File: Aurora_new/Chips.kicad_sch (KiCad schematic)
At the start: 87 parts, among them J1 UJ20-C-H-C-3-SMT-TR, J16 PPPC042LFBN-RC, J3 PPPC042LFBN-RC, J36 PPPC042LFBN-RC, J41 STEMMA QT, J50 PCB.RPSMAFRA.HT, J6 DM3AT-SF-PEJM5, U1 STM32H757BITx, U13 XBP9X-DMUS-001, U14 MS5611-01BA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

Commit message: added breakouts for xb and stlink
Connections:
- net 3V3: no longer D5.4 (VDD)
- net 3V3_MCU: now also D5.4 (VDD)
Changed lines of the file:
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@@
 	)
 	(global_label "V_OUT"
-		(shape output)
+		(shape bidirectional)
 		(at 562.61 137.16 0)
 		(fields_autoplaced yes)
@@
 		)
 		(property "Intersheetrefs" "${INTERSHEET_REFS}"
-			(at 571.28 137.16 0)
+			(at 572.3913 137.16 0)
 			(effects
 				(font
@@
 		)
 	)
-	(global_label "3V3"
+	(global_label "3V3_MCU"
 		(shape input)
 		(at 26.67 248.92 180)
@@
 		)
 		(property "Intersheetrefs" "${INTERSHEET_REFS}"
-			(at 20.1772 248.92 0)
-			(effects
-				(font
+			(at 15.1577 248.92 0)
+			(effects
+				(font

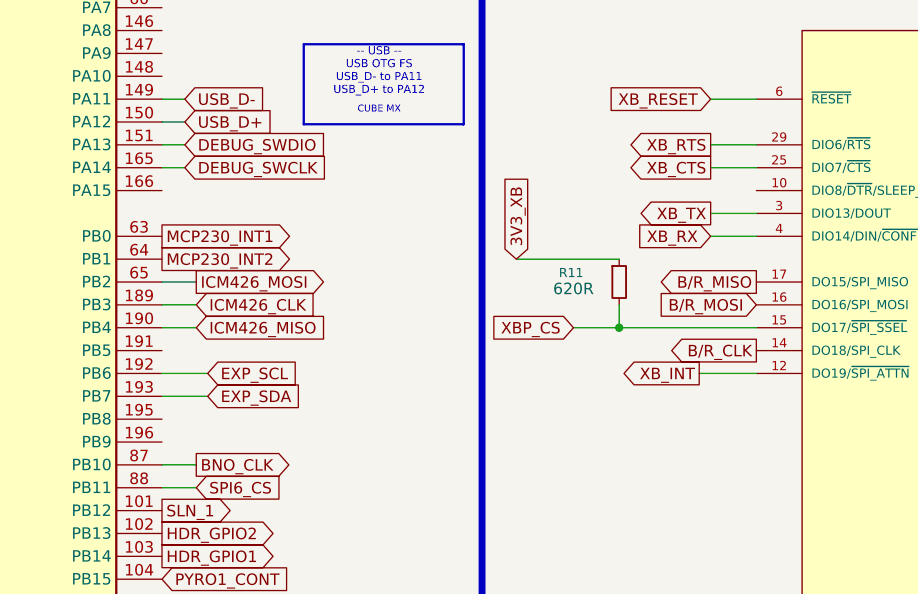
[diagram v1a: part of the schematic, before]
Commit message: fixed header pins, XB on UART
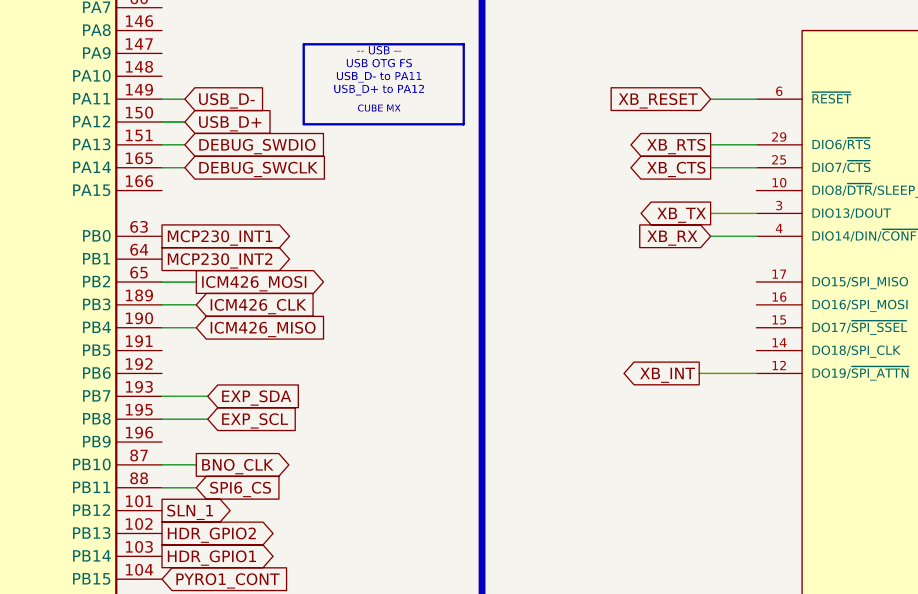
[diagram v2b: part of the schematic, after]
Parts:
- removed R11: 620R, Resistor_SMD:R_0805_2012Metric, symbol Device:R_Small
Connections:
- net B/R_CLK: no longer U13.14 (DO18/SPI_CLK)
- net B/R_MISO: no longer U13.17 (DO15/SPI_MISO)
- net B/R_MOSI: no longer U13.16 (DO16/SPI_MOSI)
- net EXP_SCL: now also U1.195 (PB8); no longer U1.192 (PB6)
- net XBP_CS: no longer U13.15 (DO17/~{SPI_SSEL})
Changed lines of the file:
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@@
 	)
 	(junction
-		(at 231.14 168.91)
-		(diameter 0)
-		(color 0 0 0 0)
-	)
-	(junction
 		(at 48.26 57.15)
 		(diameter 0)
@@
 	(wire
 		(pts
-			(xy 231.14 168.91) (xy 231.14 166.37)
-		)
-		(stroke
-			(width 0)
-			(type default)
-		)
-	)
-	(wire
-		(pts
 			(xy 478.79 341.63) (xy 478.79 347.98)
 		)
@@
 	(wire
 		(pts
-			(xy 231.14 168.91) (xy 246.38 168.91)
-		)
-		(stroke
-			(width 0)
-			(type default)
-		)
-	)
-	(wire
-		(pts
 			(xy 241.3 148.59) (xy 246.38 148.59)
 		)
@@
 	(wire
 		(pts
-			(xy 231.14 168.91) (xy 226.06 168.91)
-		)
-		(stroke
-			(width 0)
-			(type default)
-		)
-	)
-	(wire
-		(pts
 			(xy 38.1 49.53) (xy 40.64 49.53)
 		)
@@
 	(wire
 		(pts
-			(xy 180.34 173.99) (xy 185.42 173.99)
-		)
-		(stroke
-			(width 0)
-			(type default)
-		)
-	)
-	(wire
-		(pts
 			(xy 73.66 49.53) (xy 76.2 49.53)
 		)
@@
 	(wire
 		(pts
-			(xy 502.92 64.77) (xy 502.92 66.04)
+			(xy 180.34 179.07) (xy 185.42 179.07)
 		)
 		(stroke
@@
 	(wire
 		(pts
-			(xy 397.51 97.79) (xy 397.51 95.25)
+			(xy 502.92 64.77) (xy 502.92 66.04)
 		)
 		(stroke
@@
 	(wire
 		(pts
-			(xy 308.61 121.92) (xy 311.15 121.92)
+			(xy 397.51 97.79) (xy 397.51 95.25)
 		)
 		(stroke
@@
 	(wire
 		(pts
-			(xy 231.14 161.29) (xy 219.71 161.29)
+			(xy 308.61 121.92) (xy 311.15 121.92)
 		)
 		(stroke
@@
 		)
 	)
-	(global_label "B{slash}R_CLK"
-		(shape output)
-		(at 246.38 171.45 180)
-		(fields_autoplaced yes)
-		(effects
-			(font
-				(size 1.27 1.27)
-			)
-			(justify right)
-		)
-		(property "Intersheetrefs" "${INTERSHEET_REFS}"
-			(at 234.9886 171.45 0)
-			(effects
-				(font
-					(size 1.27 1.27)
-				)
-				(justify right)
-				(hide yes)
-			)
-		)
-	)
 	(global_label "BNO_NRST"
 		(shape output)
@@
 		)
 	)
-	(global_label "3V3_XB"
-		(shape input)
-		(at 219.71 161.29 90)
-		(fields_autoplaced yes)
-		(effects
-			(font
-				(size 1.27 1.27)
-			)
-			(justify left)
-		)
-		(property "Intersheetrefs" "${INTERSHEET_REFS}"
-			(at 219.71 151.3501 90)
-			(effects
-				(font
-					(size 1.27 1.27)
-				)
-				(justify left)
-				(hide yes)
-			)
-		)
-	)
 	(global_label "GPIO_B7"
 		(shape input)
@@
 		)
 	)
-	(global_label "XBP_CS"
-		(shape input)
-		(at 226.06 168.91 180)
-		(fields_autoplaced yes)
-		(effects
-			(font
-				(size 1.27 1.27)
-			)
-			(justify right)
-		)
-		(property "Intersheetrefs" "${INTERSHEET_REFS}"
-			(at 215.8782 168.91 0)
-			(effects
-				(font
-					(size 1.27 1.27)
-				)
-				(justify right)
-				(hide yes)
-			)
-		)
-	)
 	(global_label "3V3_SENS"
 		(shape input)
@@
 		)
 	)
-	(global_label "EXP_SCL"
-		(shape input)
-		(at 185.42 173.99 0)
-		(fields_autoplaced yes)
-		(effects
-			(font
-				(size 1.27 1.27)
-			)
-			(justify left)
-		)
-		(property "Intersheetrefs" "${INTERSHEET_REFS}"
-			(at 196.5089 173.99 0)
-			(effects
-				(font
-					(size 1.27 1.27)
-				)
-				(justify left)
-				(hide yes)
-			)
-		)
-	)
 	(global_label "ICM426_INT2"
 		(shape output)
@@
 		)
 	)
+	(global_label "EXP_SCL"
+		(shape input)
+		(at 185.42 179.07 0)
+		(fields_autoplaced yes)
+		(effects
+			(font
+				(size 1.27 1.27)
+			)
+			(justify left)
+		)
+		(property "Intersheetrefs" "${INTERSHEET_REFS}"
+			(at 196.5089 179.07 0)
+			(effects
+				(font
+					(size 1.27 1.27)
+				)
+				(justify left)
+				(hide yes)
+			)
+		)
+	)
 	(global_label "SD_DAT3"
 		(shape input)
@@
 		)
 	)
-	(global_label "B{slash}R_MOSI"
-		(shape input)
-		(at 246.38 166.37 180)
-		(fields_autoplaced yes)
-		(effects
-			(font
-				(size 1.27 1.27)
-			)
-			(justify right)
-		)
-		(property "Intersheetrefs" "${INTERSHEET_REFS}"
-			(at 233.9605 166.37 0)
-			(effects
-				(font
-					(size 1.27 1.27)
-				)
-				(justify right)
-				(hide yes)
-			)
-		)
-	)
 	(global_label "VDDLDO"
 		(shape input)
@@
 		)
 	)
-	(global_label "B{slash}R_MISO"
-		(shape output)
-		(at 246.38 163.83 180)
-		(fields_autoplaced yes)
-		(effects
-			(font
-				(size 1.27 1.27)
-			)
-			(justify right)
-		)
-		(property "Intersheetrefs" "${INTERSHEET_REFS}"
-			(at 233.9605 163.83 0)
-			(effects
-				(font
-					(size 1.27 1.27)
-				)
-				(justify right)
-				(hide yes)
-			)
-		)
-	)
 	(symbol
 		(lib_id "Device:C_Small")
@@
 					(unit 1)
 				)
-			)
-		)
-	)
-	(symbol
-		(lib_id "Device:R_Small")
-		(at 231.14 163.83 0)
-		(unit 1)
-		(exclude_from_sim no)
-		(in_bom yes)
-		(on_board yes)
-		(dnp no)
-		(property "Reference" "R11"
-			(at 225.806 162.814 0)
-			(effects
-				(font
-					(size 1.016 1.016)
-				)
-			)
-		)
-		(property "Value" "620R"
-			(at 226.06 164.592 0)
-			(effects
-				(font
-					(size 1.27 1.27)
-				)
-			)
-		)
-		(property "Footprint" "Resistor_SMD:R_0805_2012Metric"
-			(at 231.14 163.83 0)
-			(effects
-				(font
-					(size 1.27 1.27)
-				)
-				(hide yes)
-			)
-		)
-		(property "Datasheet" "~"
-			(at 231.14 163.83 0)
-			(effects
-				(font
-					(size 1.27 1.27)
-				)
-				(hide yes)
-			)
-		)
-		(property "Description" "Resistor, small symbol"
-			(at 231.14 163.83 0)
-			(effects
-				(font
-					(size 1.27 1.27)
-				)
-				(hide yes)
-			)
-		)
-		(property "PURCHASE-URL" "https://www.digikey.com/en/products/detail/bourns-inc/CR0805-FX-6200ELF/3785055"
-			(at 231.14 163.83 90)
-			(effects
-				(font
-					(size 1.27 1.27)
-				)
-				(hide yes)
-			)
-		)
-		(property "Price" " $0.00661"
-			(at 231.14 163.83 90)
-			(effects
-				(font
-					(size 1.27 1.27)
-				)
-				(hide yes)
-			)
-		)
-		(pin "2"
-		)
-		(pin "1"
-		)
-		(instances
-			(project "Aurora"
-				(path "/073f53a3-faa8-4419-bff2-f325850469a4/4a7b3f92-b695-4002-a887-607ce282d6cd"
-					(reference "R11")
-					(unit 1)
-				)

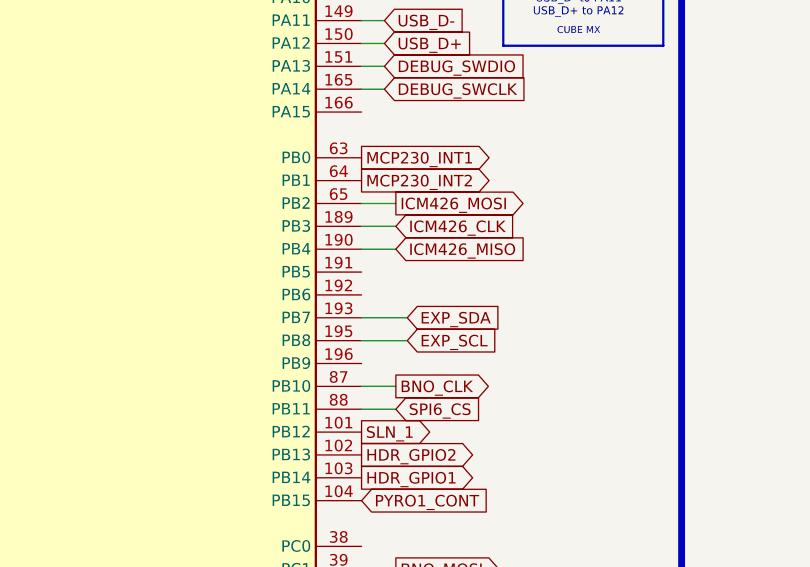
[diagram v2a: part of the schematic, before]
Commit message: NOW the xb is on UART
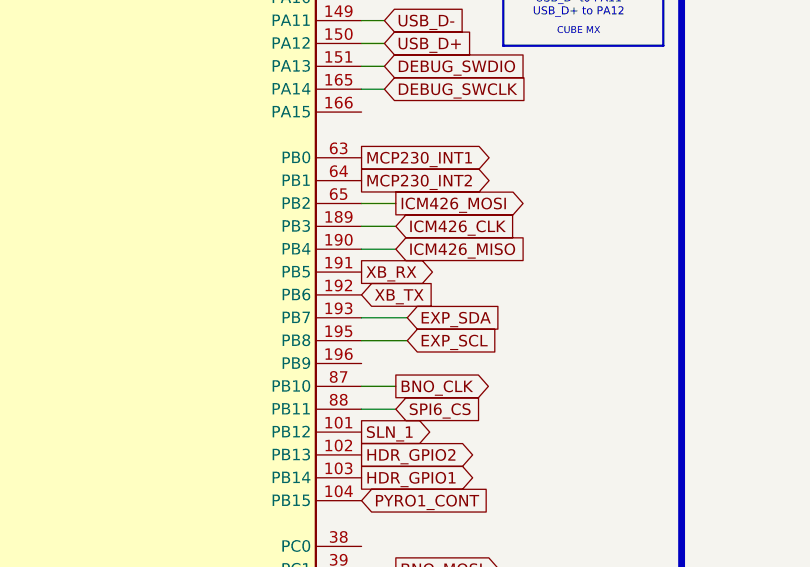
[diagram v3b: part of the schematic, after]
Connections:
- net XB_RX: now also U1.191 (PB5)
- net XB_TX: now also U1.192 (PB6)
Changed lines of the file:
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@@
+		)
+	)
+	(global_label "XB_TX"
+		(shape input)
+		(at 180.34 173.99 0)
+		(fields_autoplaced yes)
+		(effects
+			(font
+				(size 1.27 1.27)
+			)
+			(justify left)
+		)
+		(property "Intersheetrefs" "${INTERSHEET_REFS}"
+			(at 188.9494 173.99 0)
+			(effects
+				(font
+					(size 1.27 1.27)
+				)
+				(justify left)
+				(hide yes)
+			)
 		)
 	)
@@
 				(hide yes)
 			)
+		)
+	)
+	(global_label "XB_RX"
+		(shape output)
+		(at 180.34 171.45 0)
+		(fields_autoplaced yes)
+		(effects
+			(font
+				(size 1.27 1.27)
+			)
+			(justify left)
+		)
+		(property "Intersheetrefs" "${INTERSHEET_REFS}"
+			(at 189.2518 171.45 0)
+			(effects
+				(font
+					(size 1.27 1.27)
+				)
+				(justify left)
+				(hide yes)
+			)

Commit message: changes to net labelling
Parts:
- added R11: 10k, Resistor_SMD:R_0805_2012Metric, symbol Device:R_Small
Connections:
- net 3V3: now also R11.2; no longer R10.2, R12.1, R9.2
- net 3V3_SENS: now also R10.2, R12.1, R9.2
- net BNO_CLKSEL0: now also U1.156 (PH13); no longer U1.158 (PH15), U7.18 (~{H_CS})
- new net BNO_CS: R11.1, U1.158 (PH15), U7.18 (~{H_CS})
- no-connect marks 16 -> 85
